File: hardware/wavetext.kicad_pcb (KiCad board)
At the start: 2 copper layers, 150 x 30 mm, 28 parts, among them IC0 ATTINY2313A-S, P0 ISP, Q1 OPTO_NPN, SW0 DUAL_SWITCH_INV, SW1 SW_PUSH, U0 ST L78L33ACUTR

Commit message: changed design to use 10 microcontroller pins instead of 7
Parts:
- moved R10 7.06 mm to (267.2, 175.3), turned to 90 degrees
- moved U0 4.05 mm to (283.5, 172.2), turned to 0 degrees
- moved Q1 0.79 mm to (288.3, 154.9)
- moved R11 0.69 mm to (289.6, 164.5)
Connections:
- D0 pad 2: N-0000012 -> N-0000014
- D1 pad 2: N-000001 (its old number) -> N-000003
- D2 pad 2: N-000002 -> N-0000012
- D3 pad 2: N-000003 -> N-0000011
- D4 pad 2: N-000009 -> N-0000010
- D5 pad 2: N-0000012 -> N-000002
- D6 pad 2: N-000001 (its old number) -> N-0000015
- D7 pad 2: N-000002 -> N-0000016
- D8 pad 2: N-000003 -> N-0000013
- D9 pad 2: N-000009 -> N-0000017
- IC0 pad 12: N-0000011 -> N-0000014
- IC0 pad 13: N-000001 (its old number) -> N-000003
- IC0 pad 14: N-000002 -> N-0000012
- IC0 pad 15: N-000003 -> N-0000011
- IC0 pad 16: N-0000012 -> N-0000010
- IC0 pad 2: N-000009 -> N-000002
- IC0 pad 20: N-0000014 -> N-0000032
- IC0 pad 3: (no net) -> N-0000015
- IC0 pad 4: N-0000030 (its old number) -> N-0000019
- IC0 pad 5: N-0000031 -> N-0000020
- IC0 pad 6: N-000005 (its old number) -> N-0000016
- IC0 pad 7: N-000004 (its old number) -> N-0000013
- IC0 pad 8: (no net) -> N-0000017
- Q1 pad 3: N-0000011 -> N-000007
- R0 pad 2: N-0000030 (its old number) -> N-0000032
- R1 pad 2: N-0000030 (its old number) -> N-0000032
- R10 pad 1: N-0000014 -> N-0000032
- R11 pad 1: N-0000014 -> N-0000032
- R11 pad 2: N-0000011 -> N-000007
- R2 pad 2: N-0000030 (its old number) -> N-0000032
- R3 pad 2: N-0000030 (its old number) -> N-0000032
- R4 pad 2: N-0000030 (its old number) -> N-0000032
- R5 pad 2: N-0000031 -> N-0000032
- R6 pad 2: N-0000031 -> N-0000032
- R7 pad 2: N-0000031 -> N-0000032
- R8 pad 2: N-0000031 -> N-0000032
- R9 pad 2: N-0000031 -> N-0000032
- SW0 pad 1: N-000004 (its old number) -> N-0000019
- SW0 pad 3: N-000005 (its old number) -> N-0000020
- U0 pad 3: N-0000014 -> N-0000032
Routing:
- net GND: track 0.00 -> 170.8 mm
- net N-0000032: track 0.00 -> 93.0 mm
- net N-000004: track 0.00 -> 7.94 mm
- net N-000007: track 0.00 -> 6.07 mm
- net N-0000030: track 0.00 -> 4.43 mm
- net N-0000029: track 0.00 -> 4.43 mm
- net N-0000028: track 0.00 -> 4.43 mm
- net N-0000027: track 0.00 -> 4.43 mm
- net N-0000026: track 0.00 -> 4.43 mm
- net N-0000025: track 0.00 -> 4.43 mm
- net N-0000024: track 0.00 -> 4.43 mm
- net N-0000023: track 0.00 -> 4.43 mm
- net N-0000022: track 0.00 -> 4.43 mm
- net N-0000021: track 0.00 -> 4.43 mm

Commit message: completed schema and pcb layout
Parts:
- SW1: moved to B.Cu
- moved D9 49.0 mm to (238.8, 164.6)
- moved R9 49.0 mm to (238.8, 172.1)
- moved D0 47.5 mm to (187.8, 164.6)
- moved R0 47.5 mm to (187.8, 172.1)
- moved D8 38.4 mm to (233.1, 164.6)
- moved R8 38.4 mm to (233.1, 172.1)
- moved D1 36.9 mm to (193.4, 164.6)
- moved R1 36.9 mm to (193.4, 172.1)
- moved D7 27.8 mm to (227.4, 164.6)
- moved R7 27.8 mm to (227.4, 172.1)
- moved D2 26.3 mm to (199.1, 164.6)
- moved R2 26.3 mm to (199.1, 172.1)
- moved R11 22.4 mm to (267.2, 163.6), turned to 0 degrees
- moved D6 17.4 mm to (221.8, 164.6)
- moved R6 17.4 mm to (221.8, 172.1)
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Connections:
- D0 pad 2: N-0000014 -> N-000002
- D1 pad 2: N-000003 -> N-000001
- D2 pad 2: N-0000012 -> N-0000010
- D4 pad 2: N-0000010 -> N-000009
- D5 pad 2: N-000002 -> N-000003
- D6 pad 2: N-0000015 -> N-000005
- D7 pad 2: N-0000016 (its old number) -> N-0000012
- D9 pad 2: N-0000017 (its old number) -> N-0000014
- IC0 pad 12: N-0000014 -> N-0000010
- IC0 pad 13: N-000003 -> N-0000011
- IC0 pad 14: N-0000012 -> N-000009
- IC0 pad 15: N-0000011 -> N-000003
- IC0 pad 16: N-0000010 -> N-000005
- IC0 pad 17: N-0000018 (its old number) -> N-0000012
- IC0 pad 18: N-000001 -> N-0000013
- IC0 pad 19: N-000005 -> N-0000014
- IC0 pad 3: N-0000015 -> N-000001
- IC0 pad 6: N-0000016 (its old number) -> (no net)
- IC0 pad 7: N-0000013 -> (no net)
- IC0 pad 8: N-0000017 (its old number) -> N-0000015
- P0 pad 2: N-0000018 (its old number) -> N-0000012
- P0 pad 3: N-000001 -> N-0000013
- P0 pad 4: N-000005 -> N-0000014
- Q1 pad 1: GND -> N-0000015
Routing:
- net N-000002: track 0.00 -> 84.7 mm
- net N-000001: track 0.00 -> 77.3 mm
- net N-0000013: track 0.00 -> 65.0 mm
- net N-0000010: track 0.00 -> 61.9 mm
- net N-0000011: track 0.00 -> 58.6 mm
- net N-000009: track 0.00 -> 54.2 mm
- net N-000003: track 0.00 -> 50.0 mm
- net N-0000016: track 0.00 -> 48.3 mm
- net N-000005: track 0.00 -> 45.3 mm
- net N-0000012: track 0.00 -> 40.9 mm
- net GND: track 170.8 -> 207.5 mm
- net N-0000017: track 0.00 -> 27.3 mm
- net N-0000018: track 0.00 -> 24.0 mm
- net N-0000015: track 0.00 -> 20.2 mm
- net N-000004: track 7.94 -> 21.8 mm
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
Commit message: improved schematic and pcb
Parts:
- moved SW0 4.43 mm to (165.1, 163.1)
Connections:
- D0 pad 2: N-000002 -> N-0000011
- D1 pad 2: N-000001 -> N-0000012
- D3 pad 2: N-0000011 -> N-000009
- D4 pad 2: N-000009 -> N-000006
- D5 pad 2: N-000003 -> N-000008
- D6 pad 2: N-000005 -> N-0000021
- D7 pad 2: N-0000012 -> N-0000020
- D8 pad 2: N-0000013 -> N-000007
- D9 pad 2: N-0000014 -> N-0000016
- IC0 pad 11: (no net) -> N-000006
- IC0 pad 12: N-0000010 -> N-000008
- IC0 pad 13: N-0000011 -> N-0000021
- IC0 pad 14: N-000009 -> N-0000020
- IC0 pad 15: N-000003 -> N-000007
- IC0 pad 16: N-000005 -> N-0000016
- IC0 pad 17: N-0000012 -> N-000005
- IC0 pad 18: N-0000013 -> N-000001
- IC0 pad 19: N-0000014 -> N-000002
- IC0 pad 2: N-000002 -> N-000009
- IC0 pad 3: N-000001 -> N-0000010
- IC0 pad 4: N-0000017 (its old number) -> N-0000012
- IC0 pad 5: N-0000018 (its old number) -> N-0000011
- IC0 pad 6: (no net) -> N-0000015
- IC0 pad 7: (no net) -> N-0000014
- P0 pad 2: N-0000012 -> N-000005
- P0 pad 3: N-0000013 -> N-000001
- P0 pad 4: N-0000014 -> N-000002
- SW0 pad 1: N-0000017 (its old number) -> N-0000015
- SW0 pad 3: N-0000018 (its old number) -> N-0000014
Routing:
- net N-000004: track 21.8 -> 125.1 mm
- net N-0000014: track 1.93 -> 96.8 mm
- net N-000002: track 84.7 -> 0.00 mm
- net N-000001: track 77.3 -> 0.00 mm
- net N-0000015: track 0.00 -> 74.8 mm
- net N-0000013: track 65.0 -> 0.00 mm
- net N-000003: track 50.0 -> 0.00 mm
- net N-000006: track 0.00 -> 47.5 mm
- net N-000005: track 45.3 -> 0.00 mm
- net N-000008: track 0.00 -> 44.1 mm
- net N-0000021: track 0.00 -> 39.6 mm
- net N-0000012: track 40.9 -> 76.3 mm
- net N-0000020: track 0.00 -> 35.0 mm
- net N-000007: track 0.00 -> 30.5 mm
- net N-0000017 (its old number): track 27.3 -> 0.00 mm
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
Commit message: PCB
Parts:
- removed P0: ISP, CONN5_SMD
- removed R11: R, SM1206
- added C1: C, SM1206, F.Cu at (277.1, 169.0)
- added C2: C, SM1206, F.Cu at (267.1, 169.0)
- added P1: CONN_6, PIN_ARRAY-6X1, F.Cu at (299.0, 166.1)
- R0, R1, R2, R3, R4, R5, R6, R7, R8, R9: footprint SM1206 -> SM0402
- moved Q1 95.7 mm to (176.8, 164.3), turned to 90 degrees
- moved SW1 10.6 mm to (281.7, 161.3), turned to 90 degrees
- moved R10 10.5 mm to (267.2, 160.1), turned to 90 degrees
- moved U0 8.39 mm to (272.0, 169.4)
- moved R0 1.14 mm to (187.8, 170.9)
- moved R1 1.14 mm to (193.4, 170.9)
- moved R2 1.14 mm to (199.1, 170.9)
- moved R3 1.14 mm to (204.8, 170.9)
- moved R4 1.14 mm to (210.4, 170.9)
- moved R5 1.14 mm to (216.1, 170.9)
- moved R6 1.14 mm to (221.8, 170.9)
- moved R7 1.14 mm to (227.4, 170.9)
- moved R8 1.14 mm to (233.1, 170.9)
- moved R9 1.14 mm to (238.8, 170.9)
- moved D5 0.06 mm to (216.2, 164.6), turned to 270 degrees
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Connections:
- D0 pad 1: N-0000030 -> N-0000017
- D0 pad 2: N-0000011 -> N-0000028
- D1 pad 1: N-0000029 -> N-0000011
- D1 pad 2: N-0000012 (its old number) -> N-0000021
- D2 pad 1: N-0000028 -> N-0000010
- D2 pad 2: N-0000010 -> N-0000026
- D3 pad 1: N-0000026 -> N-000009
- D3 pad 2: N-000009 -> N-0000025
- D4 pad 1: N-0000031 -> N-000008
- D4 pad 2: N-000006 -> N-0000029
- D5 pad 1: N-0000025 -> N-000001
- D5 pad 2: N-000008 -> N-0000024
- D6 pad 1: N-0000024 -> N-000007
- D6 pad 2: N-0000021 -> N-0000023
- D7 pad 1: N-0000023 -> N-000006
- D7 pad 2: N-0000020 -> N-0000022
- D8 pad 1: N-0000022 -> N-000005
- D8 pad 2: N-000007 -> N-0000027
- D9 pad 1: N-0000027 -> N-000004
- D9 pad 2: N-0000016 (its old number) -> N-0000030
- IC0 pad 11: N-000006 -> N-000008
- IC0 pad 12: N-000008 -> N-000001
- IC0 pad 13: N-0000021 -> N-000007
- IC0 pad 14: N-0000020 -> N-000006
- IC0 pad 15: N-000007 -> N-000005
- IC0 pad 16: N-0000016 (its old number) -> N-000004
- IC0 pad 20: N-0000032 -> N-0000020
- IC0 pad 4: N-0000012 (its old number) -> N-0000011
- IC0 pad 5: N-0000011 -> N-0000017
- IC0 pad 8: N-0000017 -> N-000002
- Q1 pad 1: N-0000017 -> GND
- Q1 pad 3: N-0000019 (its old number) -> N-000002
- R0 pad 1: N-0000030 -> N-0000028
- R0 pad 2: N-0000032 -> GND
- R1 pad 1: N-0000029 -> N-0000021
- R1 pad 2: N-0000032 -> GND
- R10 pad 1: N-0000032 -> N-0000020
- R2 pad 1: N-0000028 -> N-0000026
- R2 pad 2: N-0000032 -> GND
- R3 pad 1: N-0000026 -> N-0000025
- R3 pad 2: N-0000032 -> GND
- R4 pad 1: N-0000031 -> N-0000029
- R4 pad 2: N-0000032 -> GND
- R5 pad 1: N-0000025 -> N-0000024
- R5 pad 2: N-0000032 -> GND
- R6 pad 1: N-0000024 -> N-0000023
- R6 pad 2: N-0000032 -> GND
- R7 pad 1: N-0000023 -> N-0000022
- R7 pad 2: N-0000032 -> GND
- R8 pad 1: N-0000022 -> N-0000027
- R8 pad 2: N-0000032 -> GND
- R9 pad 1: N-0000027 -> N-0000030
- R9 pad 2: N-0000032 -> GND
- U0 pad 1: (no net) -> VCC
- U0 pad 3: N-0000032 -> N-0000020
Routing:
- net N-0000032: track 89.8 -> 0.00 mm
- net N-0000012: track 125.1 -> 39.7 mm
- net N-0000012 (its old number): track 76.3 -> 0.00 mm
- net N-0000017: track 20.2 -> 80.6 mm
- net N-0000014: track 0.00 -> 53.1 mm
- net N-0000015: track 0.00 -> 51.4 mm
- net N-0000016: track 0.00 -> 49.3 mm
- net N-000001: track 0.00 -> 44.1 mm
- net N-0000021: track 39.6 -> 4.43 mm
- net N-000005: track 0.00 -> 30.5 mm
- net N-0000016 (its old number): track 25.6 -> 0.00 mm
- net N-000004: track 0.00 -> 25.6 mm
- net N-000003: track 48.3 -> 29.6 mm
- net N-0000020: track 35.0 -> 48.2 mm
- net N-000006: track 47.5 -> 35.0 mm
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
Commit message: rearranged pcb parts
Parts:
- SW0: footprint 3PIN_6mm -> Wackelschalter
- moved R0 17.2 mm to (171.4, 176.5)
- moved D0 17.2 mm to (171.4, 170.2)
- moved SW0 16.8 mm to (155.3, 176.8)
- moved R1 15.4 mm to (179.1, 176.5)
- moved D1 15.4 mm to (179.1, 170.2)
- moved D2 13.6 mm to (186.7, 170.2)
- moved R2 13.6 mm to (186.7, 176.5)
- moved Q1 13.1 mm to (165.1, 170.2)
- moved R3 10.8 mm to (195.6, 176.5)
- moved D3 10.7 mm to (195.6, 170.2)
- moved D4 9.14 mm to (203.2, 170.2)
- moved R4 9.14 mm to (203.2, 176.5)
- moved D5 7.73 mm to (210.8, 170.2)
- moved R5 7.69 mm to (210.8, 176.5)
- moved R6 6.51 mm to (218.4, 176.5)
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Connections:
- IC0 pad 6: N-0000019 (its old number) -> N-0000017
- SW0 pad 1: N-0000019 (its old number) -> GND
- SW0 pad 2: GND -> N-0000017
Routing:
- net N-0000010: track 76.3 -> 0.00 mm
- net N-0000019 (its old number): track 74.8 -> 0.00 mm
- net GND: track 212.9 -> 286.7 mm
- net N-000009: track 73.3 -> 0.00 mm
- net N-000008: track 68.7 -> 0.00 mm
- net N-0000018: track 96.8 -> 43.7 mm
- net N-0000017: track 0.00 -> 50.7 mm
- net N-000001: track 47.5 -> 0.00 mm
- net N-0000011: track 80.6 -> 36.4 mm
- net N-000007: track 44.1 -> 0.00 mm
- net N-0000012: track 0.00 -> 40.7 mm
- net N-000006: track 39.6 -> 0.00 mm
- net N-000005: track 35.0 -> 0.00 mm
- net N-000004: track 30.5 -> 0.00 mm
- net N-000003: track 25.6 -> 0.00 mm

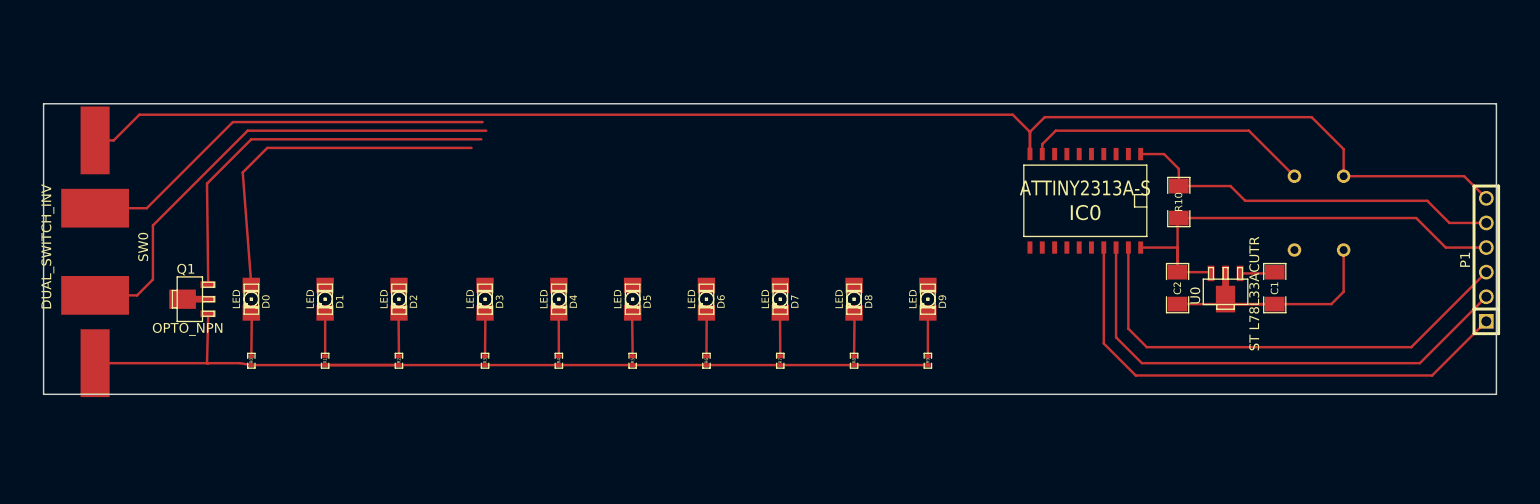
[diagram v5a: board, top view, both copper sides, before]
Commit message: Fixed pin numbering on wackelschalter.
Completed wirering on pcb.
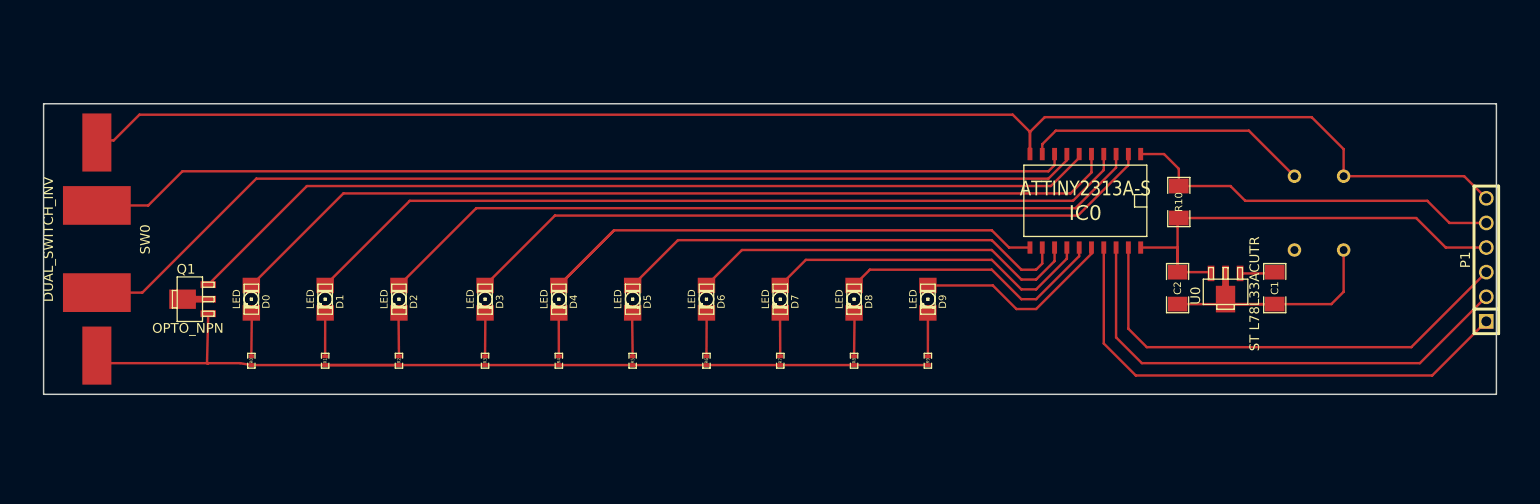
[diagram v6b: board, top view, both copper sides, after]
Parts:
- moved SW0 0.80 mm to (155.5, 176.0)
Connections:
- IC0 pad 8: N-0000012 (its old number) -> N-0000019
- Q1 pad 3: N-0000012 (its old number) -> N-0000017
- SW0 pad 1: GND -> N-0000018
- SW0 pad 2: N-0000017 -> GND
- SW0 pad 3: N-0000018 -> N-0000019
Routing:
- net N-0000019: track 0.00 -> 101.7 mm
- net N-0000010: track 0.00 -> 87.0 mm
- net N-000009: track 0.00 -> 80.5 mm
- net N-000008: track 0.00 -> 72.7 mm
- net N-0000018: track 43.7 -> 106.4 mm
- net N-000007: track 0.00 -> 59.8 mm
- net N-0000011: track 36.4 -> 93.5 mm
- net N-000001: track 0.00 -> 47.4 mm
- net N-0000017: track 50.7 -> 95.7 mm
- net N-000006: track 0.00 -> 40.9 mm
- net N-0000012 (its old number): track 40.7 -> 0.00 mm
- net N-000005: track 0.00 -> 34.4 mm
- net N-000004: track 0.00 -> 27.9 mm
- net N-000003: track 0.00 -> 20.9 mm

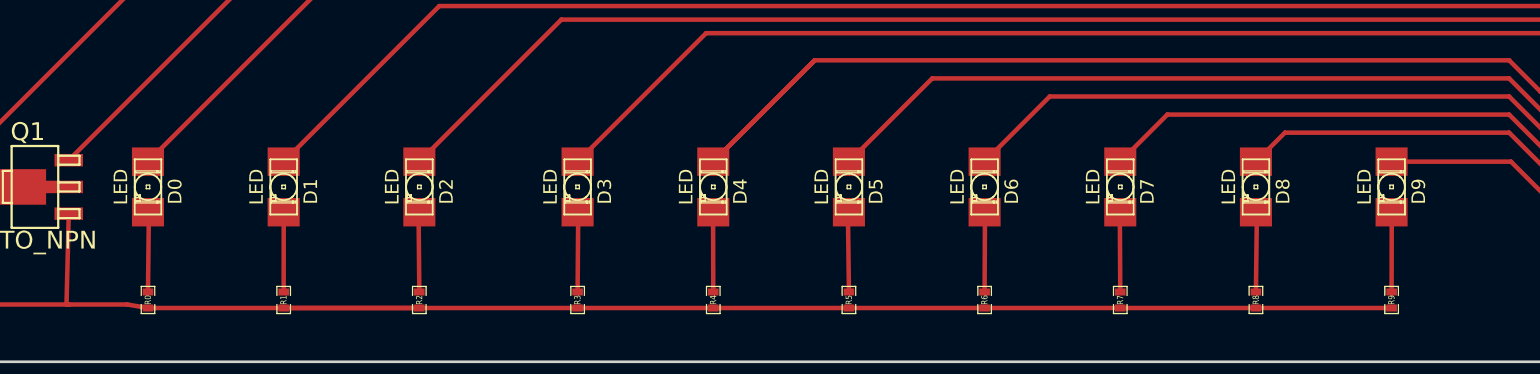
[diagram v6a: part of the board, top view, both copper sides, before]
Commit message: changed led footprint
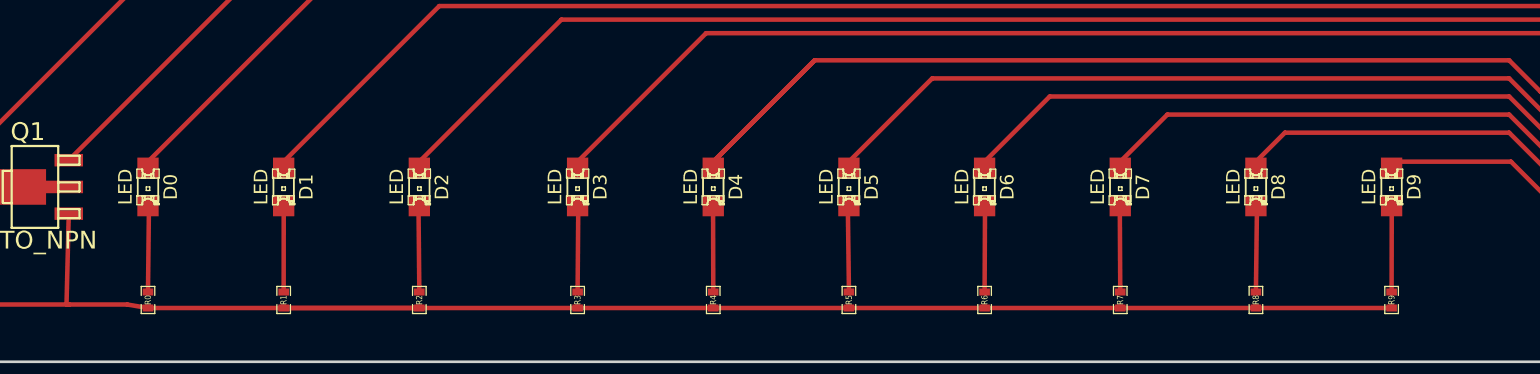
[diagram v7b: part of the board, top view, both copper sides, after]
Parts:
- D0, D1, D2, D3, D4, D5, D6, D7, D8, D9: footprint LED-1206 -> LED-0805

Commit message: PCB fertig
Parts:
- added P2: CONN_1, Powerpad, F.Cu at (274.3, 165.4)
- added P3: CONN_1, Powerpad, F.Cu at (244.1, 153.9)
- D0, D1, D2, D3, D4, D5, D6, D7, D8, D9: footprint LED-0805 -> LED
- P1: footprint PIN_ARRAY-6X1 -> PCBISP
- Q1: footprint sot89 -> Fototransistor
- SW1: footprint SW_PUSH_SMALL -> SW_PUSH_SMD; moved to F.Cu
- moved P1 14.0 mm to (300.1, 180.1), turned to 0 degrees
- moved SW1 2.69 mm to (284.4, 160.9), turned to 270 degrees
- moved C1 2.03 mm to (277.1, 171.1)
- moved C2 2.03 mm to (267.1, 171.1)
- moved U0 2.03 mm to (272.0, 171.4)
- moved Q1 2.01 mm to (165.7, 168.3), turned to 180 degrees
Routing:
- net GND: track 286.7 -> 325.7 mm
- net N-0000013: track 48.2 -> 53.7 mm
- net N-000002: track 29.6 -> 34.4 mm
- net N-0000014: track 53.1 -> 48.4 mm
- net N-0000015: track 51.4 -> 46.9 mm
- net VCC: track 3.63 -> 8.15 mm
- net N-0000018: track 106.4 -> 110.5 mm
- net N-0000016: track 49.3 -> 45.3 mm
- net N-0000012: track 39.7 -> 42.3 mm
- net N-0000017: track 95.7 -> 97.8 mm
- added copper zone on F.Cu, net GND
